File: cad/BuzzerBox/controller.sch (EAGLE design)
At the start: 87 parts, among them Q1 BSS138, Q2 BSS138

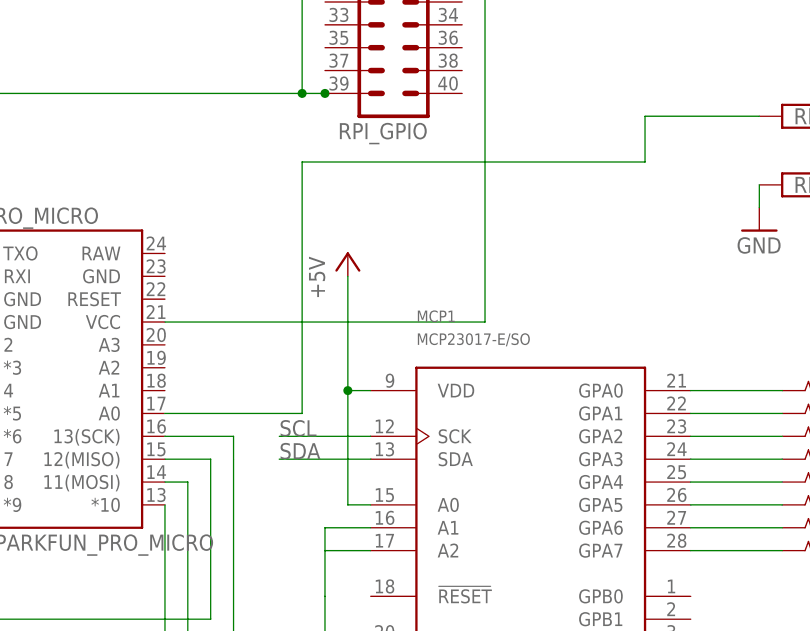
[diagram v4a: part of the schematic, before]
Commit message: Added Pullup Resistors to I2C-Bus
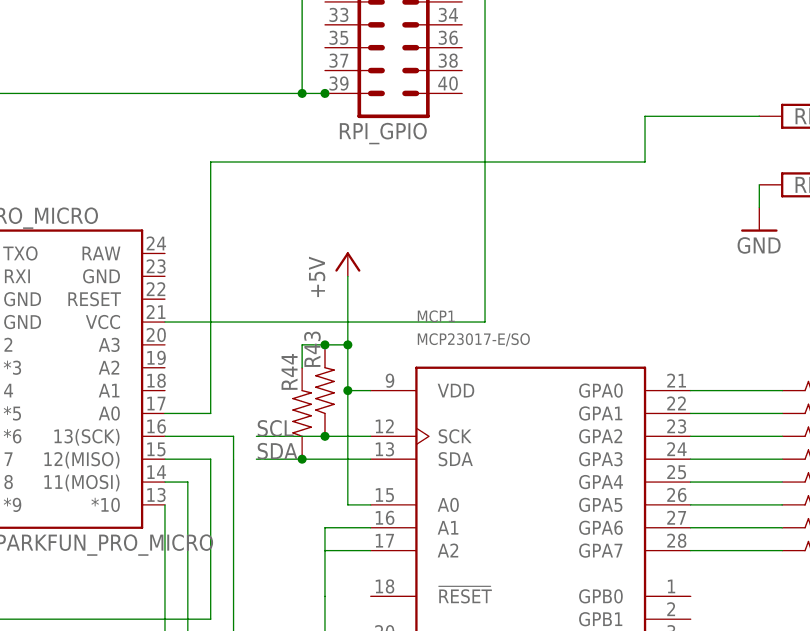
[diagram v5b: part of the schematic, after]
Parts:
- added R43, R44: (no value), SparkFun-Resistors:RESISTOR0805
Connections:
- net +5V: now also R43.2, R44.2
- net SCL: now also R43.1
- net SDA: now also R44.1
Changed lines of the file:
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@@
 <part name="RLSBT" library="con-phoenix-350" library_urn="urn:adsk.eagle:library:174" deviceset="1751248" device="" package3d_urn="urn:adsk.eagle:package:9395/1"/>
 <part name="GND25" library="supply1" library_urn="urn:adsk.eagle:library:371" deviceset="GND" device=""/>
+<part name="R43" library="SparkFun-Resistors" library_urn="urn:adsk.eagle:library:532" deviceset="RESISTOR" device="0805" package3d_urn="urn:adsk.eagle:package:39651/1" value=" "/>
+<part name="R44" library="SparkFun-Resistors" library_urn="urn:adsk.eagle:library:532" deviceset="RESISTOR" device="0805" package3d_urn="urn:adsk.eagle:package:39651/1" value=" "/>
 </parts>
 <sheets>
@@
 <instance part="GND25" gate="1" x="236.22" y="96.52" smashed="yes">
 <attribute name="VALUE" x="233.68" y="93.98" size="1.778" layer="96"/>
+</instance>
+<instance part="R43" gate="G$1" x="187.96" y="78.74" smashed="yes" rot="R90">
+<attribute name="NAME" x="187.452" y="83.312" size="1.778" layer="95" font="vector" rot="R90" align="bottom-center"/>
+<attribute name="VALUE" x="189.484" y="78.74" size="1.778" layer="96" font="vector" rot="R90" align="top-center"/>
+</instance>
+<instance part="R44" gate="G$1" x="185.42" y="76.2" smashed="yes" rot="R90">
+<attribute name="NAME" x="184.912" y="80.772" size="1.778" layer="95" font="vector" rot="R90" align="bottom-center"/>
+<attribute name="VALUE" x="186.944" y="76.2" size="1.778" layer="96" font="vector" rot="R90" align="top-center"/>
 </instance>
 </instances>
@@
 <segment>
 <pinref part="P+7" gate="1" pin="+5V"/>
-<wire x1="190.5" y1="91.44" x2="190.5" y2="78.74" width="0.1524" layer="91"/>
+<wire x1="190.5" y1="91.44" x2="190.5" y2="83.82" width="0.1524" layer="91"/>
 <pinref part="MCP1" gate="G$1" pin="VDD"/>
+<wire x1="190.5" y1="83.82" x2="190.5" y2="78.74" width="0.1524" layer="91"/>
 <wire x1="190.5" y1="78.74" x2="193.04" y2="78.74" width="0.1524" layer="91"/>
 <pinref part="MCP1" gate="G$1" pin="A0"/>
@@
 <wire x1="190.5" y1="66.04" x2="193.04" y2="66.04" width="0.1524" layer="91"/>
 <junction x="190.5" y="78.74"/>
+<pinref part="R43" gate="G$1" pin="2"/>
+<wire x1="187.96" y1="83.82" x2="190.5" y2="83.82" width="0.1524" layer="91"/>
+<junction x="190.5" y="83.82"/>
+<pinref part="R44" gate="G$1" pin="2"/>
+<wire x1="185.42" y1="81.28" x2="185.42" y2="83.82" width="0.1524" layer="91"/>
+<wire x1="185.42" y1="83.82" x2="187.96" y2="83.82" width="0.1524" layer="91"/>
+<junction x="187.96" y="83.82"/>
 </segment>
 </net>
@@
 <segment>
 <pinref part="MCP1" gate="G$1" pin="SDA"/>
-<wire x1="193.04" y1="71.12" x2="182.88" y2="71.12" width="0.1524" layer="91"/>
-<label x="182.88" y="71.12" size="1.778" layer="95"/>
+<wire x1="193.04" y1="71.12" x2="185.42" y2="71.12" width="0.1524" layer="91"/>
+<label x="180.34" y="71.12" size="1.778" layer="95"/>
+<pinref part="R44" gate="G$1" pin="1"/>
+<wire x1="185.42" y1="71.12" x2="180.34" y2="71.12" width="0.1524" layer="91"/>
+<junction x="185.42" y="71.12"/>
 </segment>
 <segment>
@@
 <segment>
 <pinref part="MCP1" gate="G$1" pin="SCK"/>
-<wire x1="193.04" y1="73.66" x2="182.88" y2="73.66" width="0.1524" layer="91"/>
-<label x="182.88" y="73.66" size="1.778" layer="95"/>
+<wire x1="193.04" y1="73.66" x2="187.96" y2="73.66" width="0.1524" layer="91"/>
+<label x="180.34" y="73.66" size="1.778" layer="95"/>
+<pinref part="R43" gate="G$1" pin="1"/>
+<wire x1="187.96" y1="73.66" x2="180.34" y2="73.66" width="0.1524" layer="91"/>
+<junction x="187.96" y="73.66"/>
 </segment>
 <segment>
@@
 <segment>
 <pinref part="PRO_MICRO" gate="G$1" pin="A0"/>
-<wire x1="170.18" y1="76.2" x2="185.42" y2="76.2" width="0.1524" layer="91"/>
-<wire x1="185.42" y1="76.2" x2="185.42" y2="104.14" width="0.1524" layer="91"/>
-<wire x1="185.42" y1="104.14" x2="223.52" y2="104.14" width="0.1524" layer="91"/>
+<wire x1="170.18" y1="76.2" x2="175.26" y2="76.2" width="0.1524" layer="91"/>
+<wire x1="175.26" y1="76.2" x2="175.26" y2="104.14" width="0.1524" layer="91"/>
+<wire x1="175.26" y1="104.14" x2="223.52" y2="104.14" width="0.1524" layer="91"/>
 <wire x1="223.52" y1="104.14" x2="223.52" y2="109.22" width="0.1524" layer="91"/>
 <pinref part="RLSBT" gate="-1" pin="K"/>

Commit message: Clean up schematic
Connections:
- net N$1 renamed D12
- net N$10 renamed D8
- net N$11 renamed D5
- net N$14 renamed D6
- net N$16 renamed D9
- net N$18 renamed GPA1
- net N$2 renamed D7
- net N$20 renamed GPA0
- net N$21 renamed D10
- net N$22 renamed D11
- net N$24 renamed GPA6
- net N$25 renamed GPA7
- net N$26 renamed GPA5
- net N$27 renamed GPA4
- net N$28 renamed GPA3
- net N$29 renamed GPA2
- net N$30 renamed GPB0
- net N$31 renamed GPB1
- net N$33 renamed B
- net N$43 renamed G
- net N$44 renamed F
- net N$47 renamed A
- net N$48 renamed E
- net N$49 renamed OE
- net N$5 renamed D13
- net N$50 renamed A0
- net N$51 renamed D
- net N$52 renamed C
- net N$53 renamed DP
- net N$54 renamed OG
- net N$55 renamed OF
- net N$56 renamed OA
- net N$57 renamed OB
- net N$58 renamed ODP
- net N$59 renamed OC
- net N$60 renamed OD
- net N$8 renamed D4
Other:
- moved on the sheet: BUZZER0-1, BUZZER0-2, BUZZER0-3, BUZZER1-1, BUZZER1-2, BUZZER1-3, BUZZER2-1, BUZZER2-2, BUZZER2-3, BUZZER3-1, BUZZER3-2, BUZZER3-3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

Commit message: Cleanup schematic
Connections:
- net GND: now also PRO_MICRO.GND

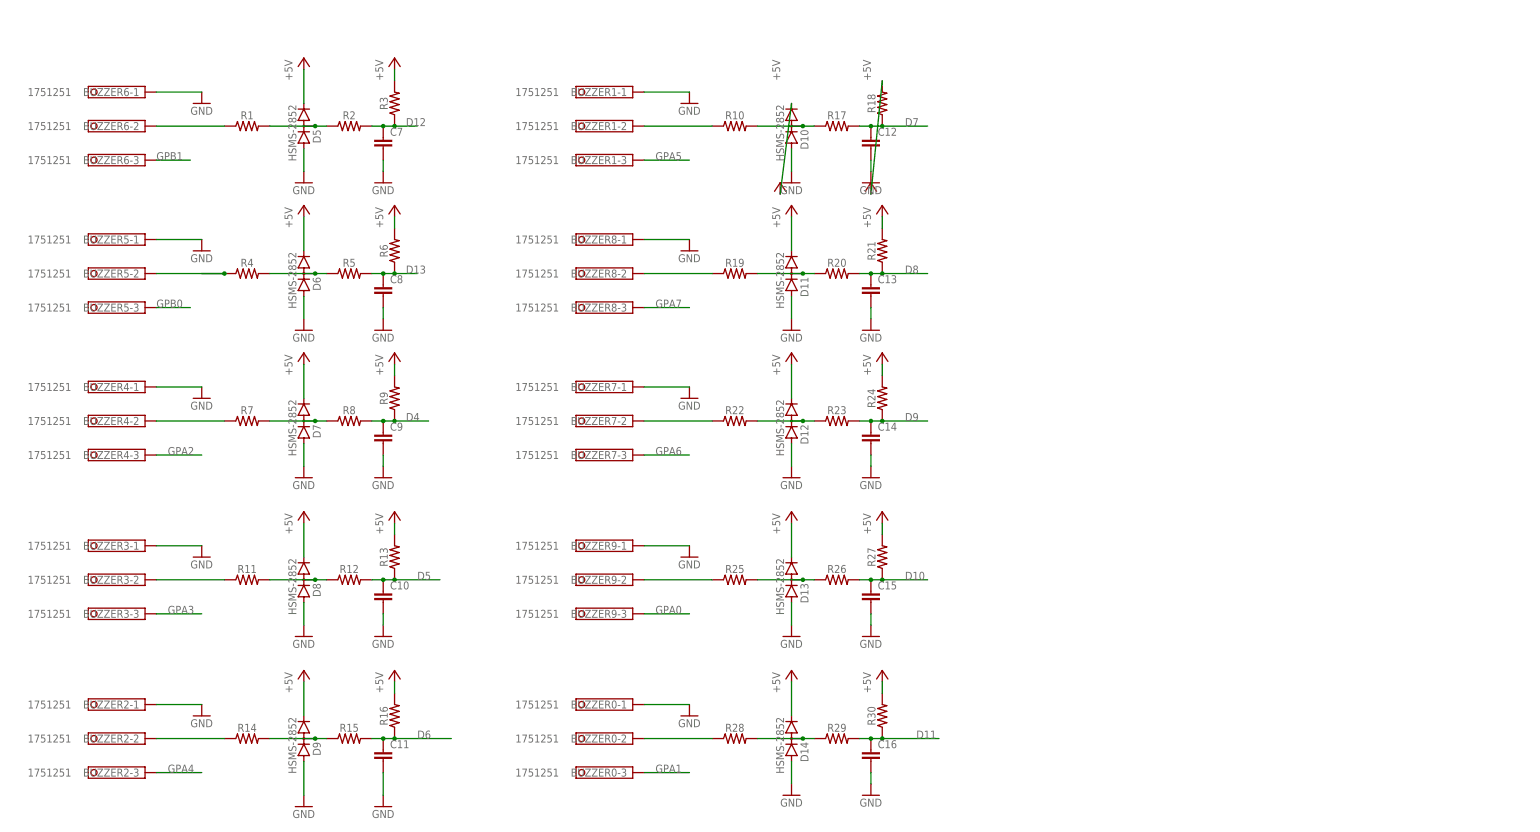
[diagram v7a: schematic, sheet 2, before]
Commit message: Added transistors for more LED power
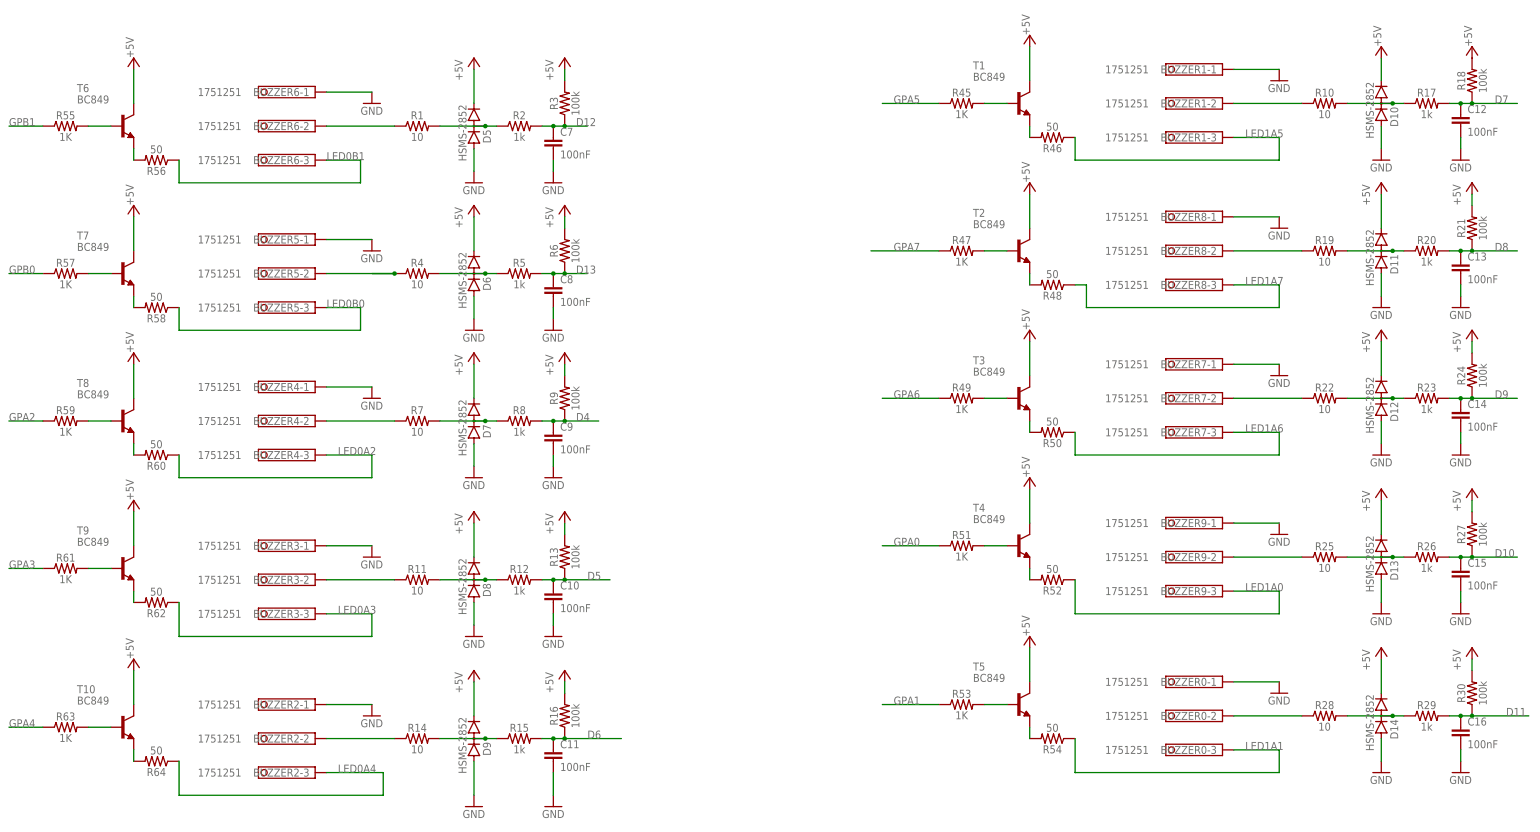
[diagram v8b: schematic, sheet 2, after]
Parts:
- added R45, R47, R49, R51, R53, R55, R57, R59, R61, R63: 1K, SparkFun-Resistors:RESISTOR0805
- added R46, R48, R50, R52, R54, R56, R58, R60, R62, R64: 50, SparkFun-Resistors:RESISTOR0805
- added T1, T10, T2, T3, T4, T5, T6, T7, T8, T9: BC849, transistor:BC849
- C10, C11, C12, C13, C14, C15, C16, C7, C8, C9: value (none) -> 100nF
- R1, R10, R11, R14, R19, R22, R25, R28, R4, R7: value (none) -> 10
- R12, R15, R17, R2, R20, R23, R26, R29, R5, R8: value (none) -> 1k
- R13, R16, R18, R21, R24, R27, R3, R30, R6, R9: value (none) -> 100k
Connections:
- new net LED0A2: BUZZER4-3.K, R60.1
- new net LED0A3: BUZZER3-3.K, R62.1
- new net LED0A4: BUZZER2-3.K, R64.1
- new net LED0B0: BUZZER5-3.K, R58.1
- new net LED0B1: BUZZER6-3.K, R56.1
- new net LED1A0: BUZZER9-3.K, R52.1
- new net LED1A1: BUZZER0-3.K, R54.1
- new net LED1A5: BUZZER1-3.K, R46.1
- new net LED1A6: BUZZER7-3.K, R50.1
- new net LED1A7: BUZZER8-3.K, R48.1
- new net N$1: R45.2, T1.B
- new net N$10: R49.2, T3.B
- new net N$11: R50.2, T3.E
- new net N$14: R51.2, T4.B
- new net N$16: R52.2, T4.E
- new net N$18: R53.2, T5.B
- new net N$2: R46.2, T1.E
- new net N$20: R54.2, T5.E
- new net N$21: R55.2, T6.B
- new net N$22: R56.2, T6.E
- new net N$24: R57.2, T7.B
- new net N$25: R58.2, T7.E
- new net N$26: R59.2, T8.B
- new net N$27: R60.2, T8.E
- new net N$28: R61.2, T9.B
- new net N$29: R62.2, T9.E
- new net N$30: R63.2, T10.B
- new net N$31: R64.2, T10.E
- new net N$5: R47.2, T2.B
- new net N$8: R48.2, T2.E
- net +5V: now also T1.C, T10.C, T2.C, T3.C, T4.C, T5.C, T6.C, T7.C, T8.C, T9.C
- net GPA0: now also R51.1; no longer BUZZER9-3.K
- net GPA1: now also R53.1; no longer BUZZER0-3.K
- net GPA2: now also R59.1; no longer BUZZER4-3.K
- net GPA3: now also R61.1; no longer BUZZER3-3.K
- net GPA4: now also R63.1; no longer BUZZER2-3.K
- net GPA5: now also R45.1; no longer BUZZER1-3.K
- net GPA6: now also R49.1; no longer BUZZER7-3.K
- net GPA7: now also R47.1; no longer BUZZER8-3.K
- net GPB0: now also R57.1; no longer BUZZER5-3.K
- net GPB1: now also R55.1; no longer BUZZER6-3.K
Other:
- moved on the sheet: BUZZER0-1, BUZZER0-2, BUZZER0-3, BUZZER1-1, BUZZER1-2, BUZZER1-3, BUZZER2-1, BUZZER2-2, BUZZER2-3, BUZZER3-1, BUZZER3-2, BUZZER3-3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
